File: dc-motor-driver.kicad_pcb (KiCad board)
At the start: 2 copper layers, 33 x 39.5 mm, 29 parts, among them J1 Conn_01x03, J10 Right, J11 RL, J12 RR, J2 MPU, J3 BAT, J4 Conn_01x03, J5 Power, J6 Left, J7 Conn_01x03, J8 FL, J9 FR, Q1 IRF7303, Q2 IRF7303

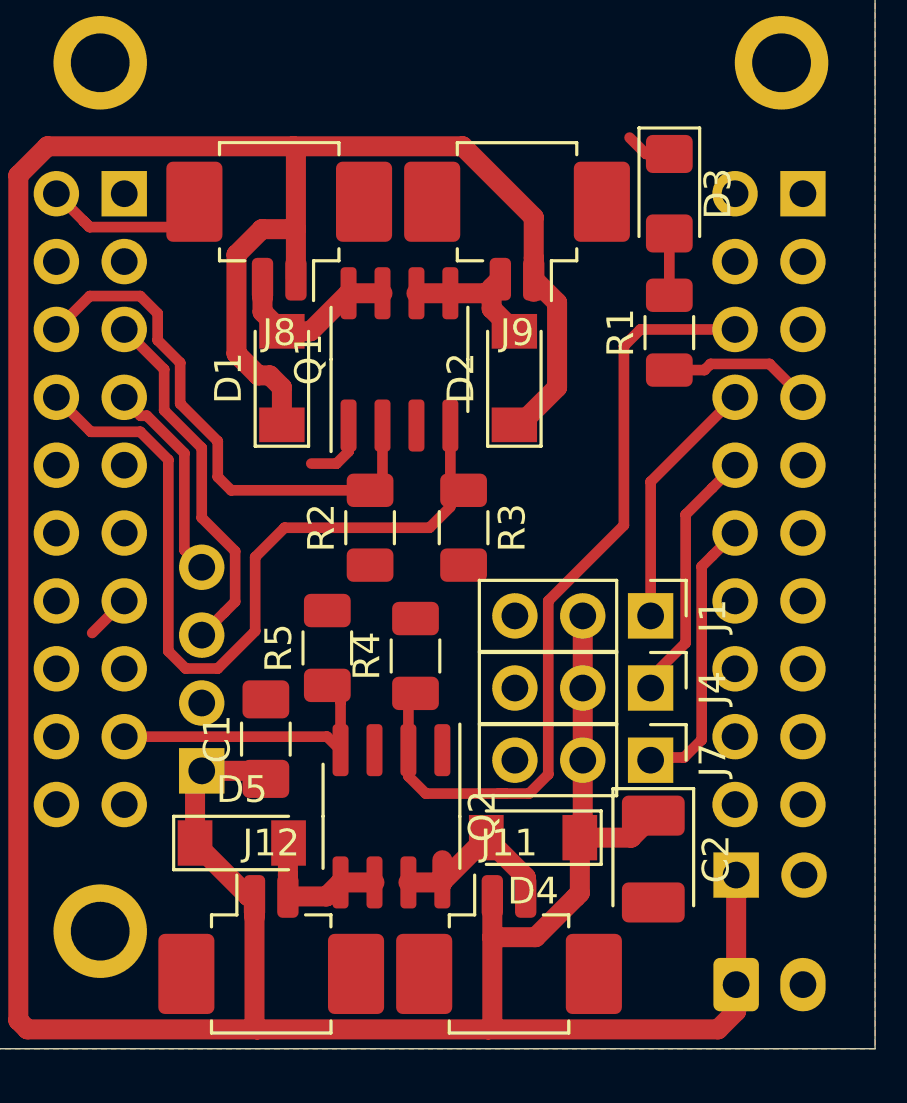
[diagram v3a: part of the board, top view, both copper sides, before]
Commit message: Adjusted the silkscreen.
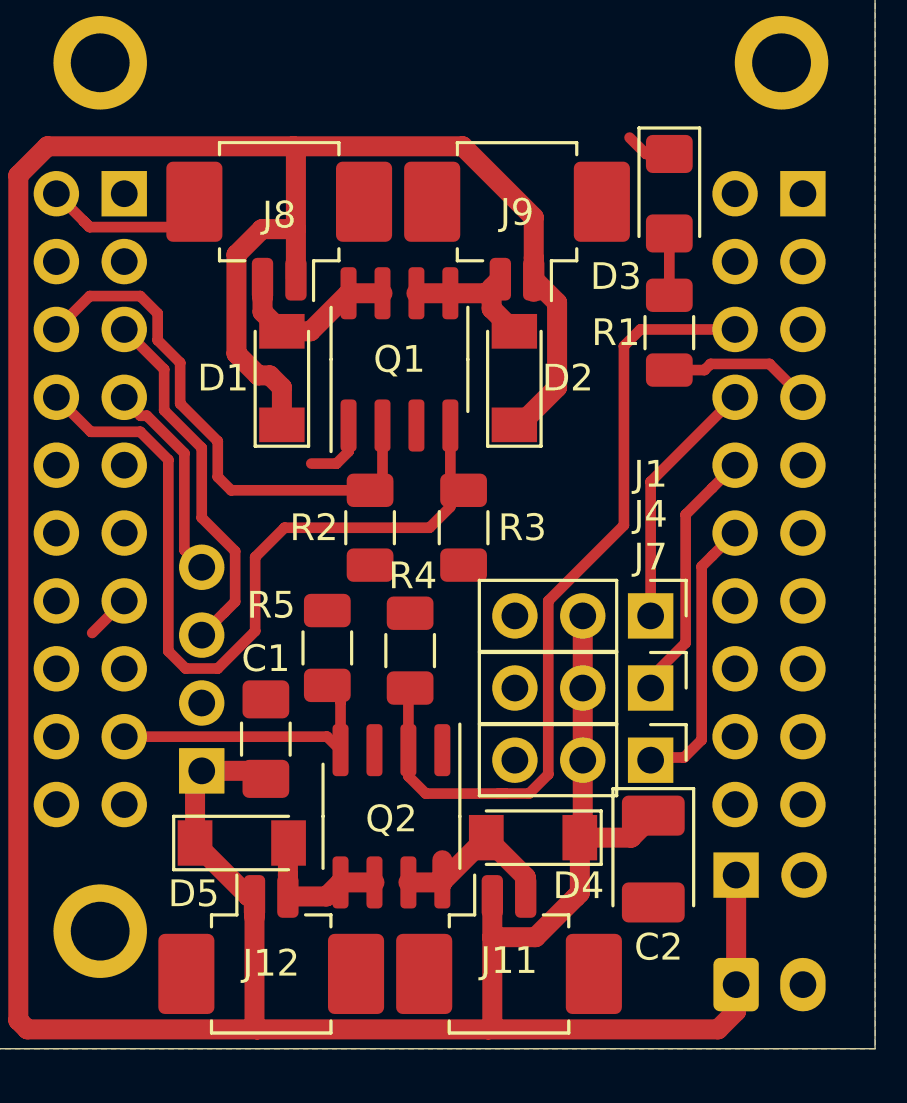
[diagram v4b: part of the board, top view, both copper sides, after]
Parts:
- moved R4 0.28 mm to (94.6, 134.6)
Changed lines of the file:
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@@
   (layers
     (0 F.Cu signal)
-    (31 B.Cu signal)
+    (31 B.Cu signal hide)
     (32 B.Adhes user hide)
     (33 F.Adhes user hide)
     (34 B.Paste user hide)
     (35 F.Paste user hide)
-    (36 B.SilkS user)
+    (36 B.SilkS user hide)
     (37 F.SilkS user)
     (38 B.Mask user hide)
@@
     (tags resistor)
     (attr smd)
-    (fp_text reference R1 (at 0 -1.82 90) (layer F.SilkS)
+    (fp_text reference R1 (at 0 -2 180) (layer F.SilkS)
       (effects (font (size 1 1) (thickness 0.15)))
     )
@@
     (tags "LED handsolder")
     (attr smd)
-    (fp_text reference D3 (at 0 -1.82 90) (layer F.SilkS)
+    (fp_text reference D3 (at 3.1 2 180) (layer F.SilkS)
       (effects (font (size 1 1) (thickness 0.15)))
     )
@@
     (tags "connector Molex PicoBlade top entry")
     (attr smd)
-    (fp_text reference J8 (at 0 -4.4) (layer F.SilkS)
+    (fp_text reference J8 (at 0 0) (layer F.SilkS)
       (effects (font (size 1 1) (thickness 0.15)))
     )
@@
     (tags "Diode Mini-MELF")
     (attr smd)
-    (fp_text reference D1 (at 0 -2 90) (layer F.SilkS)
+    (fp_text reference D1 (at 0 -2.2 180) (layer F.SilkS)
       (effects (font (size 1 1) (thickness 0.15)))
     )
@@
     (descr "Through hole straight pin header, 1x03, 2.54mm pitch, single row")
     (tags "Through hole pin header THT 1x03 2.54mm single row")
-    (fp_text reference J1 (at 0 -2.33 90) (layer F.SilkS)
+    (fp_text reference J1 (at -5.3 0) (layer F.SilkS)
       (effects (font (size 1 1) (thickness 0.15)))
     )
@@
     (descr "Through hole straight pin header, 1x03, 2.54mm pitch, single row")
     (tags "Through hole pin header THT 1x03 2.54mm single row")
-    (fp_text reference J7 (at 0 -2.33 90) (layer F.SilkS)
+    (fp_text reference J7 (at -7.6 0 180) (layer F.SilkS)
       (effects (font (size 1 1) (thickness 0.15)))
     )
@@
     (descr "Through hole straight pin header, 1x03, 2.54mm pitch, single row")
     (tags "Through hole pin header THT 1x03 2.54mm single row")
-    (fp_text reference J4 (at 0 -2.33 90) (layer F.SilkS)
+    (fp_text reference J4 (at -6.5 0 180) (layer F.SilkS)
       (effects (font (size 1 1) (thickness 0.15)))
     )
@@
     (tags "capacitor handsolder")
     (attr smd)
-    (fp_text reference C1 (at 0 -1.82 90) (layer F.SilkS)
+    (fp_text reference C1 (at 3.0125 0 180) (layer F.SilkS)
       (effects (font (size 1 1) (thickness 0.15)))
     )
@@
   )
   (module Resistor_SMD:R_1206_3216Metric (layer F.Cu)
-    (at 94.8 134.8 90)
+    (at 94.6 134.6 90)
     (descr "Resistor SMD 1206 (3216 Metric), square (rectangular) end terminal, IPC_7351 nominal, (Body size source: http://www.tortai-tech.com/upload/download/2011102023233369053.pdf), generated with kicad-footprint-generator")
     (tags resistor)
     (attr smd)
-    (fp_text reference R4 (at 0 -1.82 90) (layer F.SilkS)
+    (fp_text reference R4 (at 2.8 0.1 180) (layer F.SilkS)
       (effects (font (size 1 1) (thickness 0.15)))
     )
@@
     (descr "Through hole straight pin header, 1x02, 2.54mm pitch, single row")
     (tags "Through hole pin header THT 1x02 2.54mm single row")
-    (fp_text reference J5 (at 0 2.33 90) (layer B.SilkS)
+    (fp_text reference J5 (at 0 2.33 180) (layer B.SilkS)
       (effects (font (size 1 1) (thickness 0.15)) (justify mirror))
     )
@@
     (tags "connector Molex PicoBlade top entry")
     (attr smd)
-    (fp_text reference J12 (at 0 -4.4) (layer F.SilkS)
+    (fp_text reference J12 (at 0 0.1) (layer F.SilkS)
       (effects (font (size 1 1) (thickness 0.15)))
     )
@@
     (tags "connector Molex PicoBlade top entry")
     (attr smd)
-    (fp_text reference J9 (at 0 -4.4) (layer F.SilkS)
+    (fp_text reference J9 (at 0 0.1) (layer F.SilkS)
       (effects (font (size 1 1) (thickness 0.15)))
     )
@@
     (tags "connector Molex PicoBlade top entry")
     (attr smd)
-    (fp_text reference J11 (at 0 -4.4) (layer F.SilkS)
+    (fp_text reference J11 (at 0 0) (layer F.SilkS)
       (effects (font (size 1 1) (thickness 0.15)))
     )
@@
     (tags "capacitor tantalum")
     (attr smd)
-    (fp_text reference C2 (at 0 -2.35 90) (layer F.SilkS)
+    (fp_text reference C2 (at 3.3 -0.2 180) (layer F.SilkS)
       (effects (font (size 1 1) (thickness 0.15)))
     )
@@
     (tags "SOIC SO")
     (attr smd)
-    (fp_text reference Q2 (at 0 -3.4 90) (layer F.SilkS)
+    (fp_text reference Q2 (at 0.1 0 180) (layer F.SilkS)
       (effects (font (size 1 1) (thickness 0.15)))
     )
@@
     (tags "SOIC SO")
     (attr smd)
-    (fp_text reference Q1 (at 0 -3.4 90) (layer F.SilkS)
+    (fp_text reference Q1 (at 0 0 180) (layer F.SilkS)
       (effects (font (size 1 1) (thickness 0.15)))
     )
@@
     (descr "JST XH series connector, B2B-XH-A (http://www.jst-mfg.com/product/pdf/eng/eXH.pdf), generated with kicad-footprint-generator")
     (tags "connector JST XH vertical")
-    (fp_text reference J3 (at 1.25 3.55 180) (layer B.SilkS)
+    (fp_text reference J3 (at -3.8 0.1 180) (layer B.SilkS)
       (effects (font (size 1 1) (thickness 0.15)) (justify mirror))
     )
@@
     (tags "Diode Mini-MELF")
     (attr smd)
-    (fp_text reference D4 (at 0 -2) (layer F.SilkS)
+    (fp_text reference D4 (at -1.7 -1.8) (layer F.SilkS)
       (effects (font (size 1 1) (thickness 0.15)))
     )
@@
     (tags "Diode Mini-MELF")
     (attr smd)
-    (fp_text reference D2 (at 0 -2 90) (layer F.SilkS)
+    (fp_text reference D2 (at 0 2 180) (layer F.SilkS)
       (effects (font (size 1 1) (thickness 0.15)))
     )
@@
     (tags "Diode Mini-MELF")
     (attr smd)
-    (fp_text reference D5 (at 0 -2) (layer F.SilkS)
+    (fp_text reference D5 (at -1.8 1.9) (layer F.SilkS)
       (effects (font (size 1 1) (thickness 0.15)))
     )
@@
     (tags resistor)
     (attr smd)
-    (fp_text reference R2 (at 0 -1.82 90) (layer F.SilkS)
+    (fp_text reference R2 (at 0 -2.1 180) (layer F.SilkS)
       (effects (font (size 1 1) (thickness 0.15)))
     )
@@
     (tags resistor)
     (attr smd)
-    (fp_text reference R3 (at 0 -1.82 90) (layer F.SilkS)
+    (fp_text reference R3 (at 0 -2.2 180) (layer F.SilkS)
       (effects (font (size 1 1) (thickness 0.15)))
     )
@@
     (tags resistor)
     (attr smd)
-    (fp_text reference R5 (at 0 -1.82 90) (layer F.SilkS)
-      (effects (font (size 1 1) (thickness 0.15)))
-    )
+    (fp_text reference R5 (at 1.6 -2.1 180) (layer F.SilkS)
+      (effects (font (size 1 1) (thickness 0.15)))
+    )

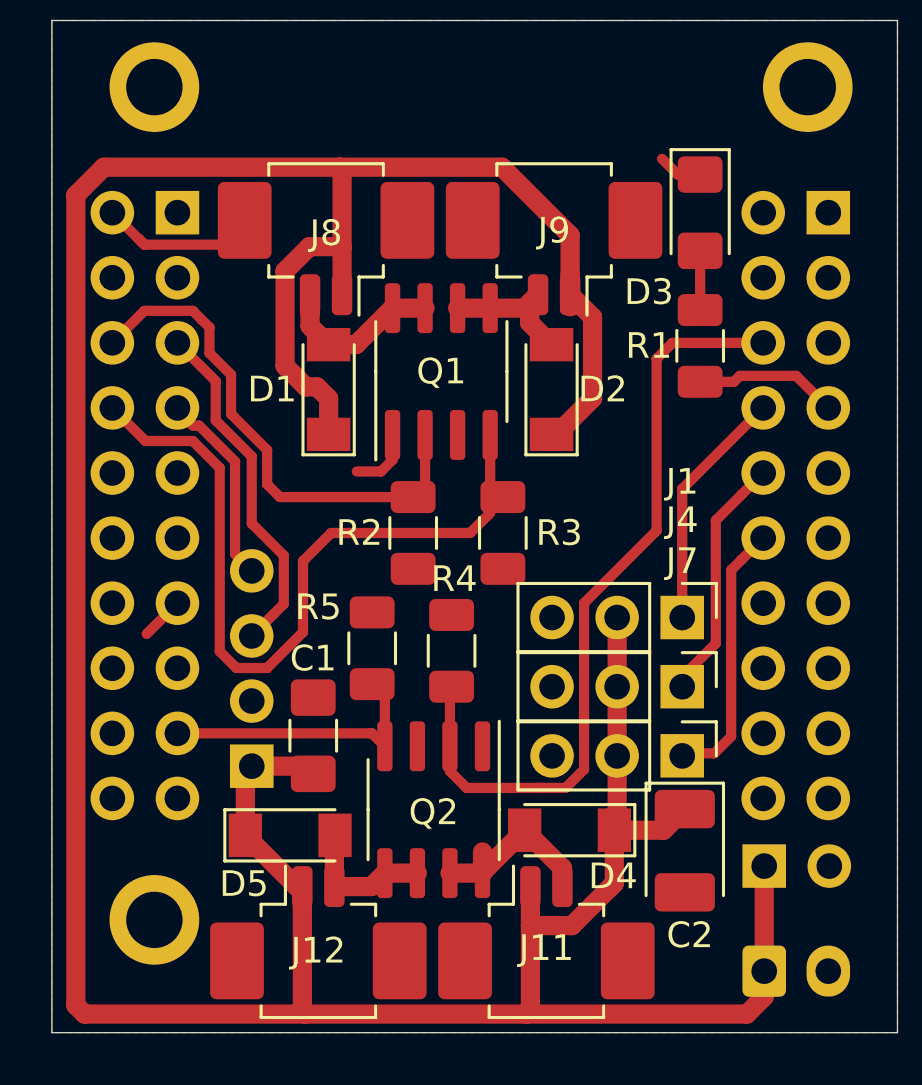
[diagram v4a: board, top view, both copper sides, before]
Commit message: Changed the molex connectors to the vertical version.
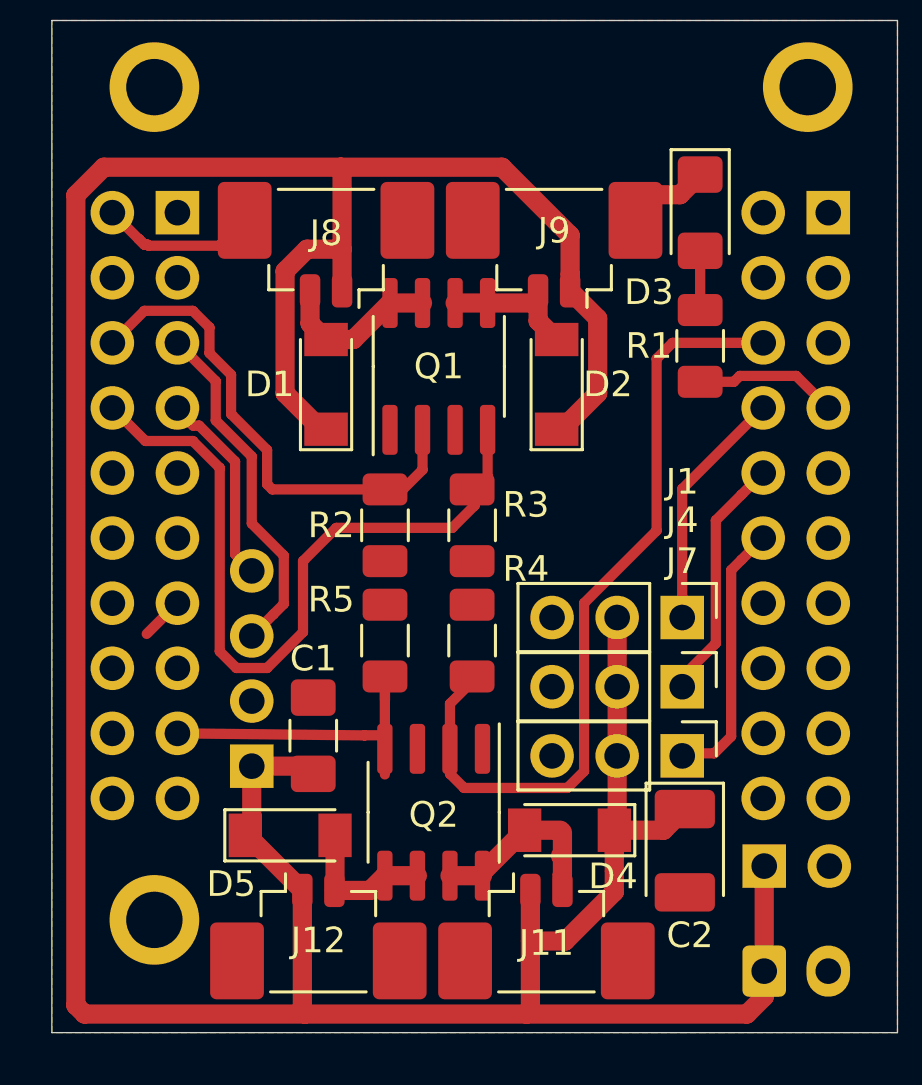
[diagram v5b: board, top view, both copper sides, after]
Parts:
- J11, J12, J8, J9: footprint Connector_Molex:Molex_PicoBlade_53261-0271_1x02-1MP_P1.25mm_Horizontal -> Connector_Molex:Molex_PicoBlade_53398-0271_1x02-1MP_P1.25mm_Vertical
- moved R3 1.24 mm to (95.4, 129.7)
- moved R2 1.14 mm to (92.0, 129.7)
- moved J11 1.00 mm to (98.3, 145.2)
- moved J12 1.00 mm to (89.4, 145.2)
- moved J8 1.00 mm to (89.7, 119.3)
- moved J9 1.00 mm to (98.6, 119.3)
- moved R4 0.89 mm to (95.4, 134.2)
- moved R5 0.58 mm to (92.0, 134.2)
- moved D2 0.28 mm to (98.7, 124.2)
- moved Q1 0.22 mm to (94.1, 123.5)
- moved D1 0.22 mm to (89.7, 124.2)
- moved Q2 0.10 mm to (93.9, 140.9)
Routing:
- net Net-(D1-Pad2): track 7.98 -> 6.51 mm
- net GND: track 12.4 -> 11.0 mm
- net /FL: track 20.8 -> 19.7 mm
- net VCC: track 147.0 -> 146.0 mm
- net /RR: track 12.2 -> 13.1 mm
- net /RL: track 31.2 -> 31.7 mm

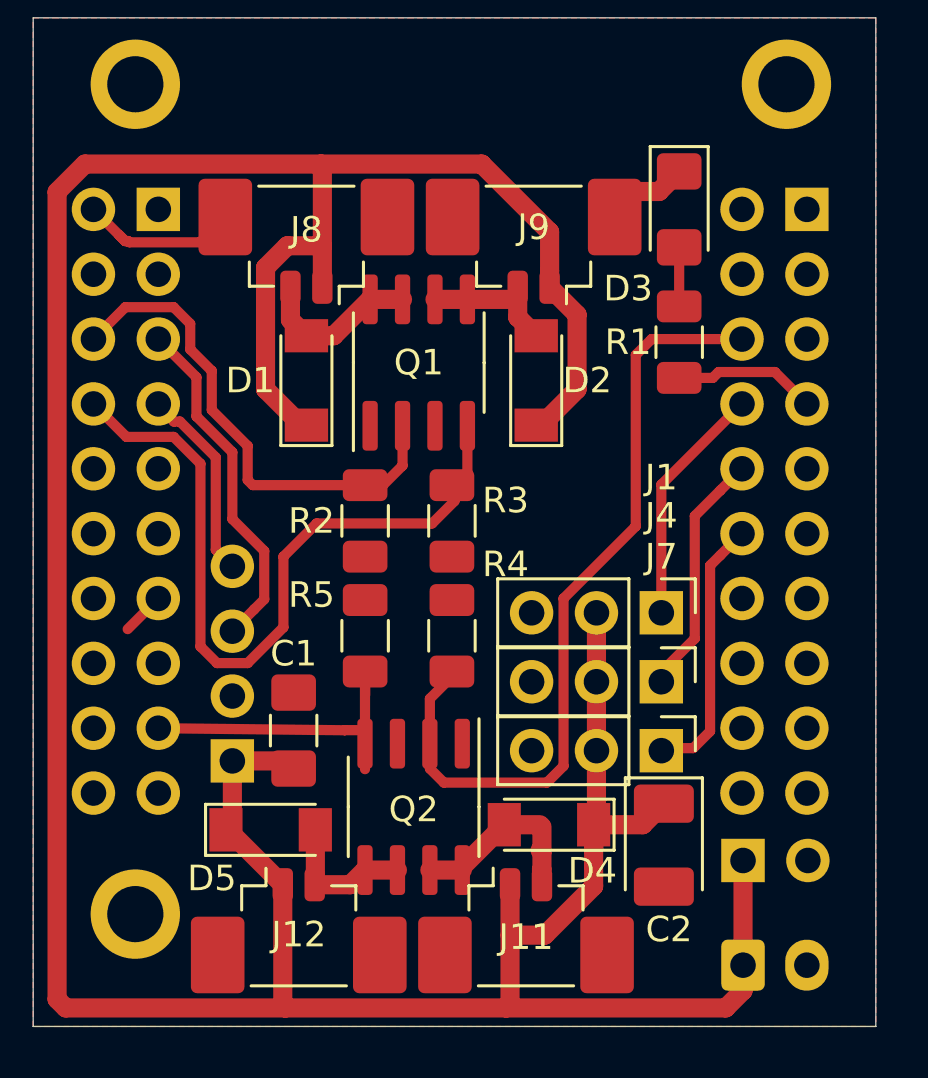
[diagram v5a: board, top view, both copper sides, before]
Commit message: Made the battery connector horizontal.
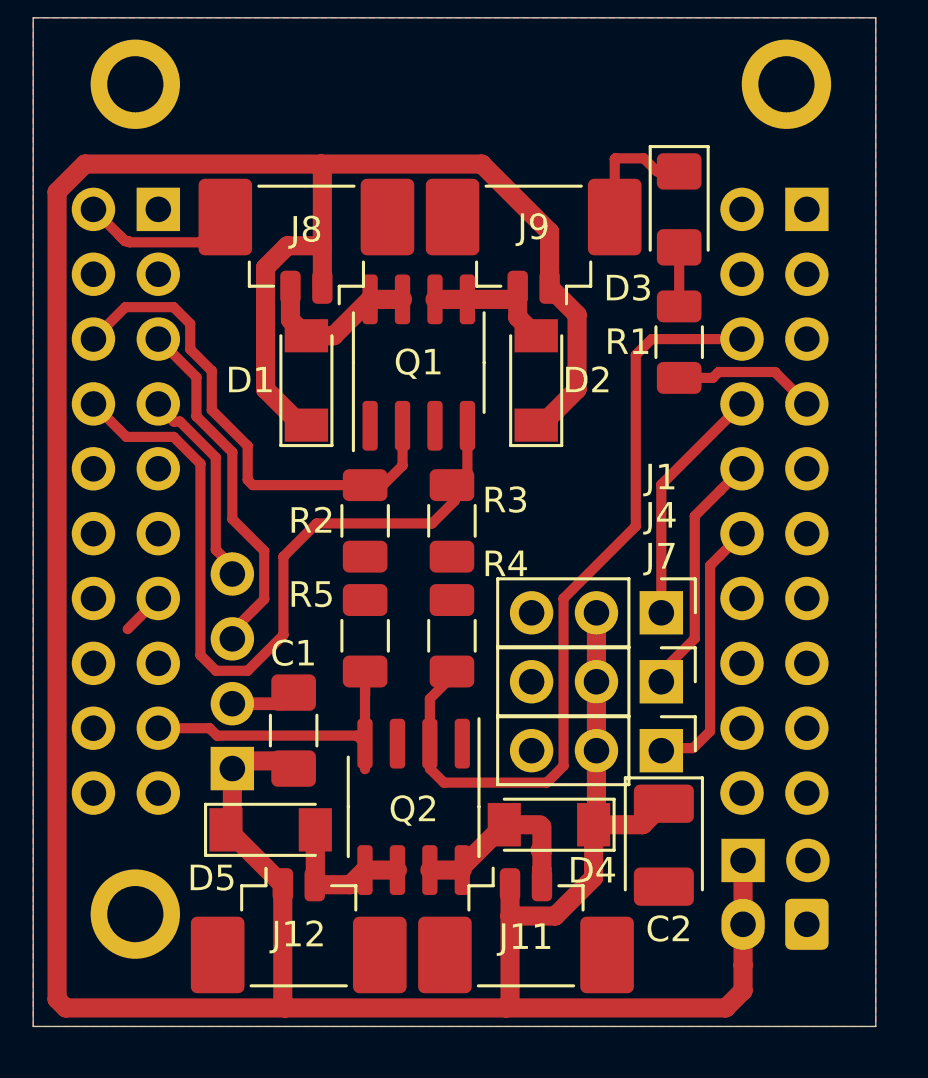
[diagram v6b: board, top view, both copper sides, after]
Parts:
- J3: footprint Connector_JST:JST_XH_B2B-XH-A_1x02_P2.50mm_Vertical -> Connector_JST:JST_XH_S2B-XH-A-1_1x02_P2.50mm_Horizontal
- moved J3 2.97 mm to (109.3, 145.5), turned to 180 degrees
- moved J2 0.30 mm to (86.8, 139.4)
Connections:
- J3 pad 1: VCC -> GND
- J3 pad 2: GND -> VCC
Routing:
- net GND: track 11.0 -> 15.7 mm
- net VCC: track 146.0 -> 144.5 mm
- net /FR: track 29.9 -> 30.6 mm
